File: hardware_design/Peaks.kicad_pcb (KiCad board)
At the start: 2 copper layers, 86.4 x 69.8 mm, 54 parts, among them J3 Eurorack Power, J8 Conn_01x07, Q1 2N3904, Q2 2N3904, U1 TL074, U2 Bluepill, U3 78l05

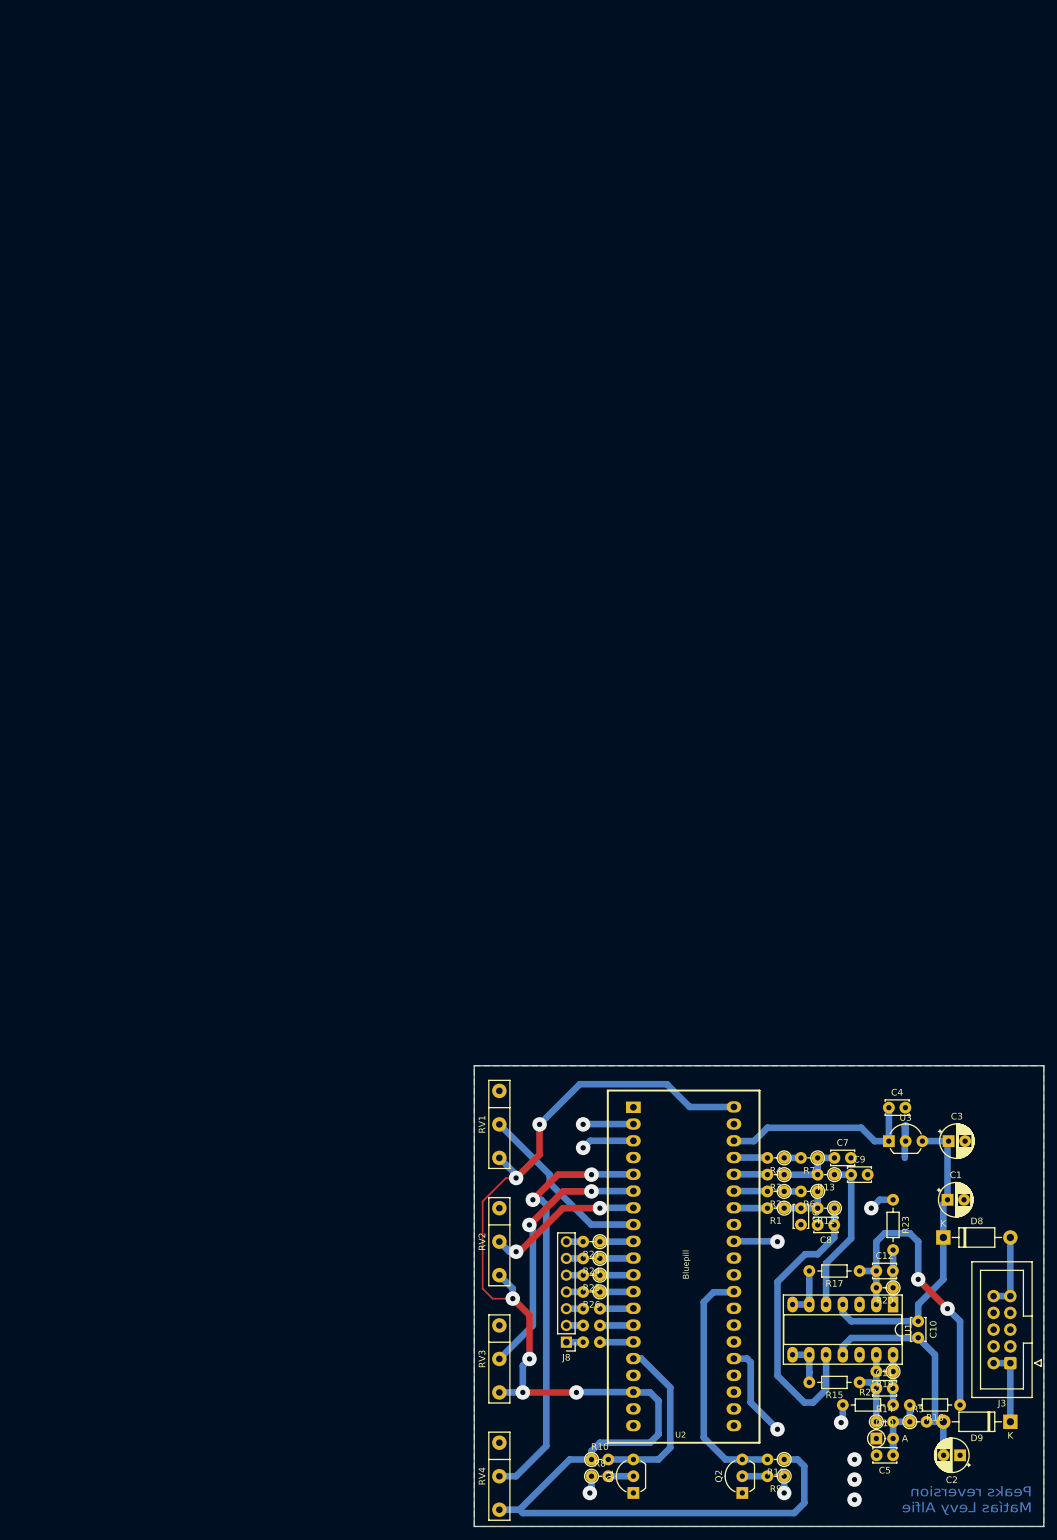
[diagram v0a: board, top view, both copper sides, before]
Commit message: Remixed hardware.
Skiff friendly (50cm depth) PCB.
Revert to using more standard KiCad footprints.
Use a 5.1V Zener diode for PWM scaling.
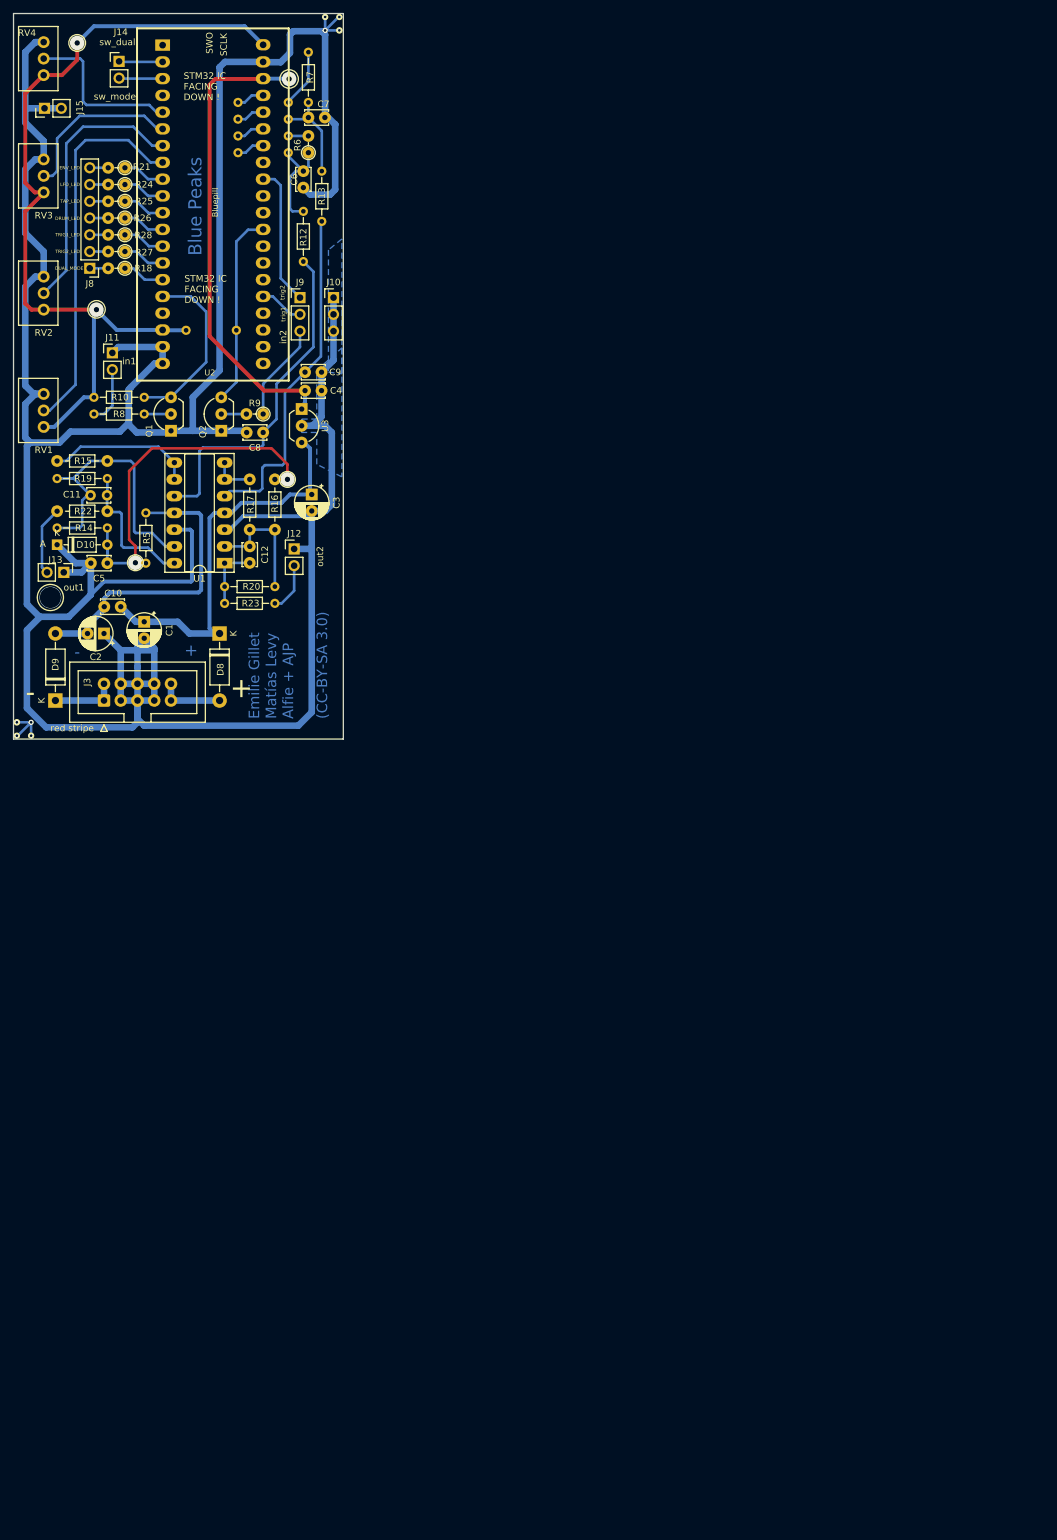
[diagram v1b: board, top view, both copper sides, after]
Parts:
- added J10: PinHeader_1x03_P2.54mm_Vertical, Connector_PinHeader_2.54mm:PinHeader_1x03_P2.54mm_Vertical, F.Cu at (48.5, -66.9)
- added J11: PinHeader_1x02_P2.54mm_Vertical, Connector_PinHeader_2.54mm:PinHeader_1x02_P2.54mm_Vertical, F.Cu at (15.0, -58.5)
- added J12: PinHeader_1x02_P2.54mm_Vertical, Connector_PinHeader_2.54mm:PinHeader_1x02_P2.54mm_Vertical, F.Cu at (42.5, -28.8)
- added J13: PinHeader_1x02_P2.54mm_Vertical, Connector_PinHeader_2.54mm:PinHeader_1x02_P2.54mm_Vertical, F.Cu at (7.62, -25.3)
- added J14: PinHeader_1x02_P2.54mm_Vertical, Connector_PinHeader_2.54mm:PinHeader_1x02_P2.54mm_Vertical, F.Cu at (16.0, -102.7)
- added J15: PinHeader_1x02_P2.54mm_Vertical, Connector_PinHeader_2.54mm:PinHeader_1x02_P2.54mm_Vertical, F.Cu at (4.70, -95.6)
- added J9: PinHeader_1x03_P2.54mm_Vertical, Connector_PinHeader_2.54mm:PinHeader_1x03_P2.54mm_Vertical, F.Cu at (43.4, -66.9)
- C11: footprint Personal:C_Disc_D3.4mm_W2.1mm_P2.50mm_Large_Pads -> Capacitor_THT:C_Disc_D3.4mm_W2.1mm_P2.50mm
- D10: value 3.6 -> 5.1; footprint Personal:D_DO-35_SOD27_P2.54mm_Vertical_AnodeUp_Large_Pads -> Diode_THT:D_DO-35_SOD27_P7.62mm_Horizontal
- R1, R11, R2, R3, R4: footprint Personal:R_Axial_DIN0204_L3.6mm_D1.6mm_P2.54mm_Vertical_Large_Pads -> Resistor_THT:R_Axial_DIN0204_L3.6mm_D1.6mm_P7.62mm_Horizontal; moved to B.Cu
- R10, R12, R13, R19, R20, R5, R7, R8: footprint Personal:R_Axial_DIN0204_L3.6mm_D1.6mm_P2.54mm_Vertical_Large_Pads -> Resistor_THT:R_Axial_DIN0204_L3.6mm_D1.6mm_P7.62mm_Horizontal
- R14: value 15k -> 21k; footprint Personal:R_Axial_DIN0204_L3.6mm_D1.6mm_P2.54mm_Vertical_Large_Pads -> Resistor_THT:R_Axial_DIN0204_L3.6mm_D1.6mm_P7.62mm_Horizontal
- R16: value 15k -> 21k
- R18, R27, R28: moved to F.Cu
- R23: footprint Personal:R_Axial_DIN0204_L3.6mm_D1.6mm_P7.62mm_Horizontal_Large_Pads -> Resistor_THT:R_Axial_DIN0204_L3.6mm_D1.6mm_P7.62mm_Horizontal
- RV1, RV2, RV3, RV4: footprint Personal:Potenciometro -> Potentiometer_THT:Potentiometer_Alps_RK097_Single_Horizontal
- moved RV4 228.1 mm to (4.57, -105.7), turned to 180 degrees
- moved RV3 194.5 mm to (4.57, -87.9), turned to 180 degrees
- moved R11 193.7 mm to (26.2, -62.0), turned to 0 degrees
- moved D10 183.8 mm to (6.60, -29.5)
- moved R14 183.8 mm to (6.60, -32.0)
- moved D9 181.4 mm to (6.35, -5.84), turned to 90 degrees
- moved R22 180.4 mm to (6.60, -34.5)
- moved R15 180.3 mm to (14.2, -42.2)
- moved C11 180.3 mm to (11.7, -37.0)
- moved R19 180.3 mm to (14.2, -39.5)
- moved C5 180.2 mm to (14.2, -26.7)
- moved C2 179.9 mm to (13.7, -16.0)
- moved Q2 179.4 mm to (31.5, -46.7)
- moved R9 179.4 mm to (37.8, -49.3)
- moved J8 178.1 mm to (11.6, -71.4)
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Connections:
- net +3V3 renamed 3.3V
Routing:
- net GND: track 7.42 -> 535.8 mm, vias 3 -> 8
- net 3.3V: track 204.6 -> 127.0 mm, vias 6 -> 2
- net /REF_-3.6: track 11.4 -> 57.3 mm, vias 0 -> 2
- net +5V: track 30.3 -> 71.4 mm, vias 0 -> 1
- net /POT_4: track 64.8 -> 25.0 mm, vias 2 -> 0
- net Net-(C11-Pad1): track 13.1 -> 46.0 mm
- net /POT_1: track 27.4 -> 57.2 mm
- net Net-(C9-Pad1): track 23.8 -> 52.3 mm
- net Net-(C12-Pad1): track 46.9 -> 18.8 mm, vias 2 -> 0
- net /POT_2: track 23.7 -> 41.0 mm, vias 2 -> 0
- net Net-(R15-Pad2): track 6.73 -> 22.2 mm
- net /POT_3: track 40.5 -> 25.5 mm, vias 2 -> 0
- net /SW_TRIG2: track 6.63 -> 21.5 mm, vias 1 -> 0
- net +12V: track 46.4 -> 61.1 mm
- net Net-(C11-Pad2): track 7.62 -> 21.3 mm
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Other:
- board size 86.4 x 69.8 mm -> 50 x 110 mm
- net class Default: clearance 0.2 -> 0.6; trace_width 0.25 -> 0.4
- net class GND added: clearance 0.6, trace_width 1, via_dia 1, via_drill 0.4
- net class POWER added: clearance 0.6, trace_width 0.6, via_dia 0.8, via_drill 0.4
- rule trace_clearance: 0.2 -> 0.6
- board text added: "+"
- board text added: "-"
- board text added: "Blue Peaks"
- board text added: "Corner marker to help calibration when plotting with FlatCam. Remove if sending to a PCB fab."
- board text added: "DRUM_LED"
- board text added: "DUAL_MODE"
- board text added: "ENV_LED"
- board text added: "Emilie Gillet Matías Levy Alfie + AJP (CC-BY-SA 3.0)"
- board text added: "LFO_LED"
- board text added: "Leave the 5V leg of C4 long to attach a jumper wire."
- board text added: "M3 screw hole to secure board to front panel, 3.2 mm diameter"
- board text added: "SCLK"
- board text added: "STM32 IC FACING DOWN !"
- board text added: "SWO"
- board text added: "TAP_LED"
- board text added: "TODO: Fix the orientaion of Q1, Q2, U3 and U1 and the Blue Pill (U2). Everything is on the 'wrong' side for a single sided board. When building the current PCB, you need to flip orientation of Q1, Q2, U3 and U1 (!!) and mount Blue Pill (U2) on the 'wrong side' of the boards, or alternatively 'upside down' (STM32 facing toward the PCB)."
- board text added: "TODO: Make power socket+diodes+caps more central to make space for 4xLED mounts and the out1 pin header along left edge (currently the out1 pin header is too close to the 4xLEDs when they are mounted in the panel)"
- board text added: "TODO: Mount points for 4 mode LEDs along the left edge here ? Jump a ribbon cable from pin header J8 to another pin header here."
- board text added: "TRIG1_LED"
- board text added: "TRIG2_LED"
- board text added: "There is no 'ground plane', but if that's your thing feel free to add one using a filled zone."
- board text added: "Vias attached to R5 and R16 are for a jumper wire."
- board text added: "in1"
- board text added: "in2"
- board text added: "out1"
- board text added: "out2"
- board text added: "red stripe"
- board text added: "sw_dual"
- board text added: "sw_mode"
- board text added: "trig1"
- board text added: "trig2"
- board text removed: "Peaks reversion Matías Levy Alfie"
